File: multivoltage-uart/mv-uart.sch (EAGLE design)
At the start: 39 parts, among them SW1 DIP_SP6T, U1 IP4234CZ6, U2 CP2105-GM, U3 LDO_SHD_ADJ-AP2127K-ADJ, X1 MINI-USB-SHIELD-UX60-MB-5ST

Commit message: mv-uart: Use SP6T flash *without* OFF position
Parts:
- SW1: LINK http://www.digikey.com/product-detail/en/copal-electronics-inc/SS-10-16NP-LE/563-1080-ND/948391 -> http://www.digikey.com/product-detail/en/copal-electronics-inc/SS-10-16SP-L-AE/563-1082-ND/948393; MANUFACTURERPARTNUMBER SS-10-16NP-LE -> SS-10-16SP-L-AE; SOURCEPARTNUMBER 563-1080-ND -> 563-1082-ND
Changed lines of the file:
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@@
 <attribute name="CLASS" value="UNKNOWN CLASS"/>
 <attribute name="DESCRIPTION" value="Dip Switch SP6T 6 Position Through Hole Rotary with Shaft Actuator 100mA 5VDC"/>
-<attribute name="LINK" value="http://www.digikey.com/product-detail/en/copal-electronics-inc/SS-10-16NP-LE/563-1080-ND/948391"/>
+<attribute name="LINK" value="http://www.digikey.com/product-detail/en/copal-electronics-inc/SS-10-16SP-L-AE/563-1082-ND/948393"/>
 <attribute name="MANUFACTURER" value="Copal Electronics Inc."/>
-<attribute name="MANUFACTURERPARTNUMBER" value="SS-10-16NP-LE"/>
-<attribute name="POPULATED" value="TRUE"/>
-<attribute name="ROHSCERTIFICATE" value="UNKNOWN ROHS CERTIFICATE"/>
-<attribute name="SOURCE" value="DIGIKEY"/>
-<attribute name="SOURCEPARTNUMBER" value="563-1080-ND"/>
+<attribute name="MANUFACTURERPARTNUMBER" value="SS-10-16SP-L-AE"/>
+<attribute name="POPULATED" value="TRUE"/>
+<attribute name="ROHSCERTIFICATE" value="UNKNOWN ROHS CERTIFICATE"/>
+<attribute name="SOURCE" value="DIGIKEY"/>
+<attribute name="SOURCEPARTNUMBER" value="563-1082-ND"/>
 </part>
 <part name="U3" library="ldo" deviceset="LDO_SHD_ADJ" device="-AP2127K-ADJ">
@@
 </instance>
 <instance part="SW1" gate="G$1" x="60.96" y="30.48">
+<attribute name="LINK" x="60.96" y="30.48" size="1.778" layer="96" display="off"/>
 <attribute name="DESCRIPTION" x="60.96" y="30.48" size="1.778" layer="96" display="off"/>
 <attribute name="MANUFACTURER" x="60.96" y="30.48" size="1.778" layer="96" display="off"/>
@@
 <attribute name="POPULATED" x="60.96" y="30.48" size="1.778" layer="96" display="off"/>
 <attribute name="CLASS" x="60.96" y="30.48" size="1.778" layer="96" display="off"/>
-<attribute name="LINK" x="60.96" y="30.48" size="1.778" layer="96" display="off"/>
 </instance>
 <instance part="U3" gate="G$1" x="58.42" y="60.96">

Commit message: mv-uart: Add digikey attributes for various 2.54mm hedaers
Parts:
- JP1: DESCRIPTION NO DESCRIPTION -> 4 Positions Header, Unshrouded, Breakaway Connector 0.100" 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; LINK UNKNOWN LINK -> http://www.digikey.com/product-detail/en/harwin-inc/M20-999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; MANUFACTURER UNKNOWN MANUFACTURER -> Harwin Inc.; MANUFACTURERPARTNUMBER UNKNOWN MANUFACTURER PART NUMBER -> M20-9990445; SOURCE UNKNOWN SOURCE -> DIGIKEY; SOURCEPARTNUMBER UNKNOWN SOURCE PART NUMBER -> 952-2265-ND
- JP2, JP3: DESCRIPTION NO DESCRIPTION -> 6 Positions Header, Unshrouded, Breakaway Connector 0.100" 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; LINK UNKNOWN LINK -> http://www.digikey.com/product-detail/en/harwin-inc/M20-996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; MANUFACTURER UNKNOWN MANUFACTURER -> Harwin Inc.; MANUFACTURERPARTNUMBER UNKNOWN MANUFACTURER PART NUMBER -> M20-9960645; SOURCE UNKNOWN SOURCE -> DIGIKEY; SOURCEPARTNUMBER UNKNOWN SOURCE PART NUMBER -> 952-2247-ND
- JP5: DESCRIPTION NO DESCRIPTION -> 7 Positions Header, Unshrouded, Breakaway Connector 0.100" 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; LINK UNKNOWN LINK -> http://www.digikey.com/product-detail/en/sullins-connector-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; MANUFACTURER UNKNOWN MANUFACTURER -> Sullins Connector Solutions; MANUFACTURERPARTNUMBER UNKNOWN MANUFACTURER PART NUMBER -> PRPC007SAAN-RC; SOURCE UNKNOWN SOURCE -> DIGIKEY; SOURCEPARTNUMBER UNKNOWN SOURCE PART NUMBER -> S1011EC-07-ND
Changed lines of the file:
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@@
 <part name="JP2" library="pinhead" deviceset="PINHD-1X6" device="/90">
 <attribute name="CLASS" value="CONNECTOR\JUMPER"/>
-<attribute name="DESCRIPTION" value="NO DESCRIPTION"/>
-<attribute name="LINK" value="UNKNOWN LINK"/>
-<attribute name="MANUFACTURER" value="UNKNOWN MANUFACTURER"/>
-<attribute name="MANUFACTURERPARTNUMBER" value="UNKNOWN MANUFACTURER PART NUMBER"/>
+<attribute name="DESCRIPTION" value="6 Positions Header, Unshrouded, Breakaway Connector 0.100&quot; (2.54mm) Through Hole, Right Angle Gold"/>
+<attribute name="LINK" value="http://www.digikey.com/product-detail/en/harwin-inc/M20-9960645/952-2247-ND/3728211"/>
+<attribute name="MANUFACTURER" value="Harwin Inc."/>
+<attribute name="MANUFACTURERPARTNUMBER" value="M20-9960645"/>
 <attribute name="POPULATED" value="TRUE"/>
 <attribute name="ROHSCERTIFICATE" value="UNKNOWN ROHS CERTIFICATE"/>
-<attribute name="SOURCE" value="UNKNOWN SOURCE"/>
-<attribute name="SOURCEPARTNUMBER" value="UNKNOWN SOURCE PART NUMBER"/>
+<attribute name="SOURCE" value="DIGIKEY"/>
+<attribute name="SOURCEPARTNUMBER" value="952-2247-ND"/>
 </part>
 <part name="JP3" library="pinhead" deviceset="PINHD-1X6" device="/90">
 <attribute name="CLASS" value="CONNECTOR\JUMPER"/>
-<attribute name="DESCRIPTION" value="NO DESCRIPTION"/>
-<attribute name="LINK" value="UNKNOWN LINK"/>
-<attribute name="MANUFACTURER" value="UNKNOWN MANUFACTURER"/>
-<attribute name="MANUFACTURERPARTNUMBER" value="UNKNOWN MANUFACTURER PART NUMBER"/>
+<attribute name="DESCRIPTION" value="6 Positions Header, Unshrouded, Breakaway Connector 0.100&quot; (2.54mm) Through Hole, Right Angle Gold"/>
+<attribute name="LINK" value="http://www.digikey.com/product-detail/en/harwin-inc/M20-9960645/952-2247-ND/3728211"/>
+<attribute name="MANUFACTURER" value="Harwin Inc."/>
+<attribute name="MANUFACTURERPARTNUMBER" value="M20-9960645"/>
 <attribute name="POPULATED" value="TRUE"/>
 <attribute name="ROHSCERTIFICATE" value="UNKNOWN ROHS CERTIFICATE"/>
-<attribute name="SOURCE" value="UNKNOWN SOURCE"/>
-<attribute name="SOURCEPARTNUMBER" value="UNKNOWN SOURCE PART NUMBER"/>
+<attribute name="SOURCE" value="DIGIKEY"/>
+<attribute name="SOURCEPARTNUMBER" value="952-2247-ND"/>
 </part>
 <part name="GND11" library="supply1" deviceset="GND" device=""/>
@@
 <part name="JP1" library="pinhead" deviceset="PINHD-1X4" device="">
 <attribute name="CLASS" value="CONNECTOR\JUMPER"/>
-<attribute name="DESCRIPTION" value="NO DESCRIPTION"/>
-<attribute name="LINK" value="UNKNOWN LINK"/>
-<attribute name="MANUFACTURER" value="UNKNOWN MANUFACTURER"/>
-<attribute name="MANUFACTURERPARTNUMBER" value="UNKNOWN MANUFACTURER PART NUMBER"/>
+<attribute name="DESCRIPTION" value="4 Positions Header, Unshrouded, Breakaway Connector 0.100&quot; (2.54mm) Through Hole Gold"/>
+<attribute name="LINK" value="http://www.digikey.com/product-detail/en/harwin-inc/M20-9990445/952-2265-ND/3728229"/>
+<attribute name="MANUFACTURER" value="Harwin Inc."/>
+<attribute name="MANUFACTURERPARTNUMBER" value="M20-9990445"/>
 <attribute name="POPULATED" value="TRUE"/>
 <attribute name="ROHSCERTIFICATE" value="UNKNOWN ROHS CERTIFICATE"/>
-<attribute name="SOURCE" value="UNKNOWN SOURCE"/>
-<attribute name="SOURCEPARTNUMBER" value="UNKNOWN SOURCE PART NUMBER"/>
+<attribute name="SOURCE" value="DIGIKEY"/>
+<attribute name="SOURCEPARTNUMBER" value="952-2265-ND"/>
 </part>
 <part name="GND13" library="supply1" deviceset="GND" device=""/>
@@
 <part name="JP5" library="pinhead" deviceset="PINHD-1X7" device="">
 <attribute name="CLASS" value="CONNECTOR\JUMPER"/>
-<attribute name="DESCRIPTION" value="NO DESCRIPTION"/>
-<attribute name="LINK" value="UNKNOWN LINK"/>
-<attribute name="MANUFACTURER" value="UNKNOWN MANUFACTURER"/>
-<attribute name="MANUFACTURERPARTNUMBER" value="UNKNOWN MANUFACTURER PART NUMBER"/>
+<attribute name="DESCRIPTION" value="7 Positions Header, Unshrouded, Breakaway Connector 0.100&quot; (2.54mm) Through Hole Gold"/>
+<attribute name="LINK" value="http://www.digikey.com/product-detail/en/sullins-connector-solutions/PRPC007SAAN-RC/S1011EC-07-ND/2775247"/>
+<attribute name="MANUFACTURER" value="Sullins Connector Solutions"/>
+<attribute name="MANUFACTURERPARTNUMBER" value="PRPC007SAAN-RC"/>
 <attribute name="POPULATED" value="TRUE"/>
 <attribute name="ROHSCERTIFICATE" value="UNKNOWN ROHS CERTIFICATE"/>
-<attribute name="SOURCE" value="UNKNOWN SOURCE"/>
-<attribute name="SOURCEPARTNUMBER" value="UNKNOWN SOURCE PART NUMBER"/>
+<attribute name="SOURCE" value="DIGIKEY"/>
+<attribute name="SOURCEPARTNUMBER" value="S1011EC-07-ND"/>
 </part>
 <part name="GND16" library="supply1" deviceset="GND" device=""/>

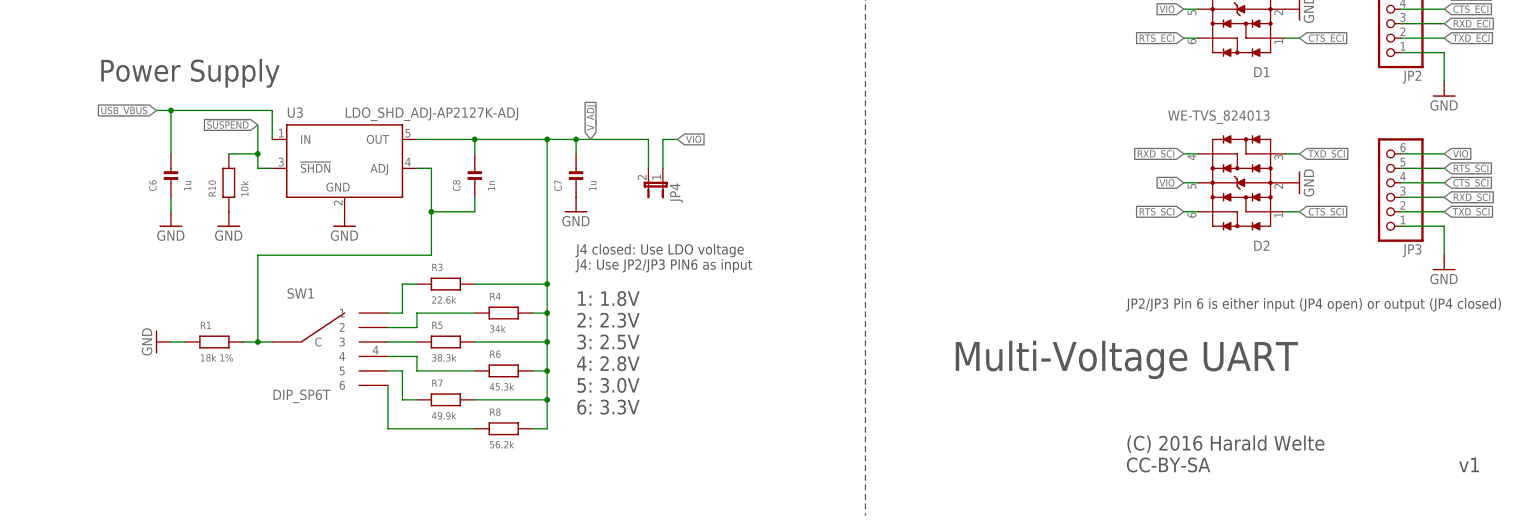
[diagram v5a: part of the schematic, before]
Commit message: mv-uart: Fix 'board doesn't enumerate if JP4 is closed" issue
Make sure the LDO is always powered up, so the CP2105 internal and
external !RESET pull-ups are towards an active VIO voltage, rather than
one that is switched off by !SUSPEND and thus keeps the CP2105 in reset.

Closes: #1870 (https://osmocom.org/issues/1870)
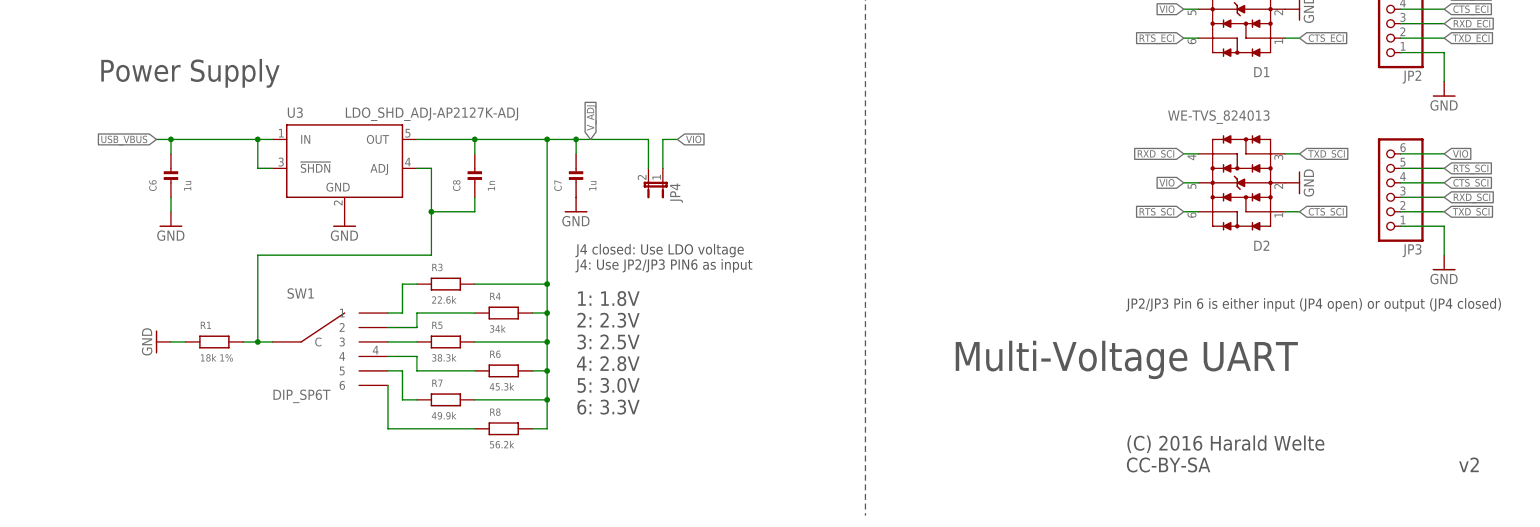
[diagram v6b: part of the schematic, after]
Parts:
- removed R10: 10k, rc-sysmocom:RESISTOR_0603
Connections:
- net !SUSPEND: no longer R10.2, U3.!SHDN
- net GND: no longer R10.1
- net USB_VBUS: now also U3.!SHDN
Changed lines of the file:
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@@
 <schematic xreflabel="%F%N/%S.%C%R" xrefpart="/%S.%C%R">
 <attributes>
-<attribute name="VERSION" value="v1"/>
+<attribute name="VERSION" value="v2"/>
 </attributes>
 <variantdefs>
@@
 </part>
 <part name="GND9" library="supply1" deviceset="GND" device=""/>
-<part name="R10" library="rc-sysmocom" deviceset="RESISTOR" device="_0603" value="10k">
-<attribute name="CLASS" value="RESISTOR"/>
-<attribute name="DESCRIPTION" value="RES SMD 10K OHM 5% 1/10W 0603"/>
-<attribute name="LINK" value="http://www.digikey.com/product-detail/en/samsung-electro-mechanics-america-inc/RC1608J103CS/1276-5086-1-ND/3968058"/>
-<attribute name="MANUFACTURER" value="Samsung Electro-Mechanics America, Inc."/>
-<attribute name="MANUFACTURERPARTNUMBER" value="RC1608J103CS"/>
-<attribute name="POPULATED" value="TRUE"/>
-<attribute name="ROHSCERTIFICATE" value="UNKNOWN ROHS CERTIFICATE"/>
-<attribute name="SOURCE" value="DIGIKEY"/>
-<attribute name="SOURCEPARTNUMBER" value="1276-5086-1-ND"/>
-</part>
-<part name="GND10" library="supply1" deviceset="GND" device=""/>
 <part name="JP2" library="pinhead" deviceset="PINHD-1X6" device="/90">
 <attribute name="CLASS" value="CONNECTOR\JUMPER"/>
@@
 </instance>
 <instance part="GND9" gate="1" x="40.64" y="101.6"/>
-<instance part="R10" gate="G$1" x="38.1" y="58.42" rot="R90">
-<attribute name="DESCRIPTION" x="38.1" y="58.42" size="1.778" layer="96" display="off"/>
-<attribute name="MANUFACTURER" x="38.1" y="58.42" size="1.778" layer="96" display="off"/>
-<attribute name="MANUFACTURERPARTNUMBER" x="38.1" y="58.42" size="1.778" layer="96" display="off"/>
-<attribute name="SOURCE" x="38.1" y="58.42" size="1.778" layer="96" display="off"/>
-<attribute name="SOURCEPARTNUMBER" x="38.1" y="58.42" size="1.778" layer="96" display="off"/>
-<attribute name="ROHSCERTIFICATE" x="38.1" y="58.42" size="1.778" layer="96" display="off"/>
-<attribute name="POPULATED" x="38.1" y="58.42" size="1.778" layer="96" display="off"/>
-<attribute name="CLASS" x="38.1" y="58.42" size="1.778" layer="96" display="off"/>
-<attribute name="LINK" x="38.1" y="58.42" size="1.778" layer="96" display="off"/>
-</instance>
-<instance part="GND10" gate="1" x="38.1" y="50.8"/>
 <instance part="JP2" gate="A" x="241.3" y="88.9" rot="R180">
 <attribute name="DESCRIPTION" x="241.3" y="88.9" size="1.778" layer="96" display="off"/>
@@
 <segment>
 <pinref part="U3" gate="G$1" pin="IN"/>
-<wire x1="45.72" y1="66.04" x2="45.72" y2="71.12" width="0.1524" layer="91"/>
-<wire x1="45.72" y1="71.12" x2="27.94" y2="71.12" width="0.1524" layer="91"/>
+<wire x1="45.72" y1="66.04" x2="43.18" y2="66.04" width="0.1524" layer="91"/>
 <pinref part="C6" gate="G$1" pin="2"/>
-<wire x1="27.94" y1="71.12" x2="25.4" y2="71.12" width="0.1524" layer="91"/>
-<wire x1="27.94" y1="63.5" x2="27.94" y2="71.12" width="0.1524" layer="91"/>
-<junction x="27.94" y="71.12"/>
-<label x="25.4" y="71.12" size="1.27" layer="95" rot="R180" xref="yes"/>
+<wire x1="43.18" y1="66.04" x2="27.94" y2="66.04" width="0.1524" layer="91"/>
+<wire x1="27.94" y1="66.04" x2="25.4" y2="66.04" width="0.1524" layer="91"/>
+<wire x1="27.94" y1="63.5" x2="27.94" y2="66.04" width="0.1524" layer="91"/>
+<junction x="27.94" y="66.04"/>
+<label x="25.4" y="66.04" size="1.27" layer="95" rot="R180" xref="yes"/>
+<pinref part="U3" gate="G$1" pin="!SHDN"/>
+<wire x1="45.72" y1="60.96" x2="43.18" y2="60.96" width="0.1524" layer="91"/>
+<wire x1="43.18" y1="60.96" x2="43.18" y2="66.04" width="0.1524" layer="91"/>
+<junction x="43.18" y="66.04"/>
 </segment>
 <segment>
@@
 <pinref part="GND9" gate="1" pin="GND"/>
 <wire x1="40.64" y1="106.68" x2="40.64" y2="104.14" width="0.1524" layer="91"/>
-</segment>
-<segment>
-<pinref part="R10" gate="G$1" pin="1"/>
-<pinref part="GND10" gate="1" pin="GND"/>
 </segment>
 <segment>
@@
 <net name="!SUSPEND" class="0">
 <segment>
-<pinref part="U3" gate="G$1" pin="!SHDN"/>
-<wire x1="45.72" y1="60.96" x2="43.18" y2="60.96" width="0.1524" layer="91"/>
-<wire x1="43.18" y1="60.96" x2="43.18" y2="63.5" width="0.1524" layer="91"/>
-<label x="43.18" y="68.58" size="1.27" layer="95" rot="R180" xref="yes"/>
-<pinref part="R10" gate="G$1" pin="2"/>
-<wire x1="43.18" y1="63.5" x2="43.18" y2="68.58" width="0.1524" layer="91"/>
-<wire x1="38.1" y1="63.5" x2="43.18" y2="63.5" width="0.1524" layer="91"/>
-<junction x="43.18" y="63.5"/>
-</segment>
-<segment>
 <pinref part="U2" gate="A" pin="!SUSPEND/RI_SCI"/>
